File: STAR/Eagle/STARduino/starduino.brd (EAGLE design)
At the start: 59.7 x 38.2 mm, 52 parts, among them J1 J30J-25, U1 PCA9515A, U10 PCA9306DCT, U11 CC2, U12 SSCMNNN015PA2A3, U2 ATSAMD21G18, U3 MAX31725MTA+, U4 MC74VHC1GT125, U5 DS3231MZ+, U6 MC14504BDTG, U7 BMX055, U8 ADXL375BCCZ, U9 TCA9535_RTW_24

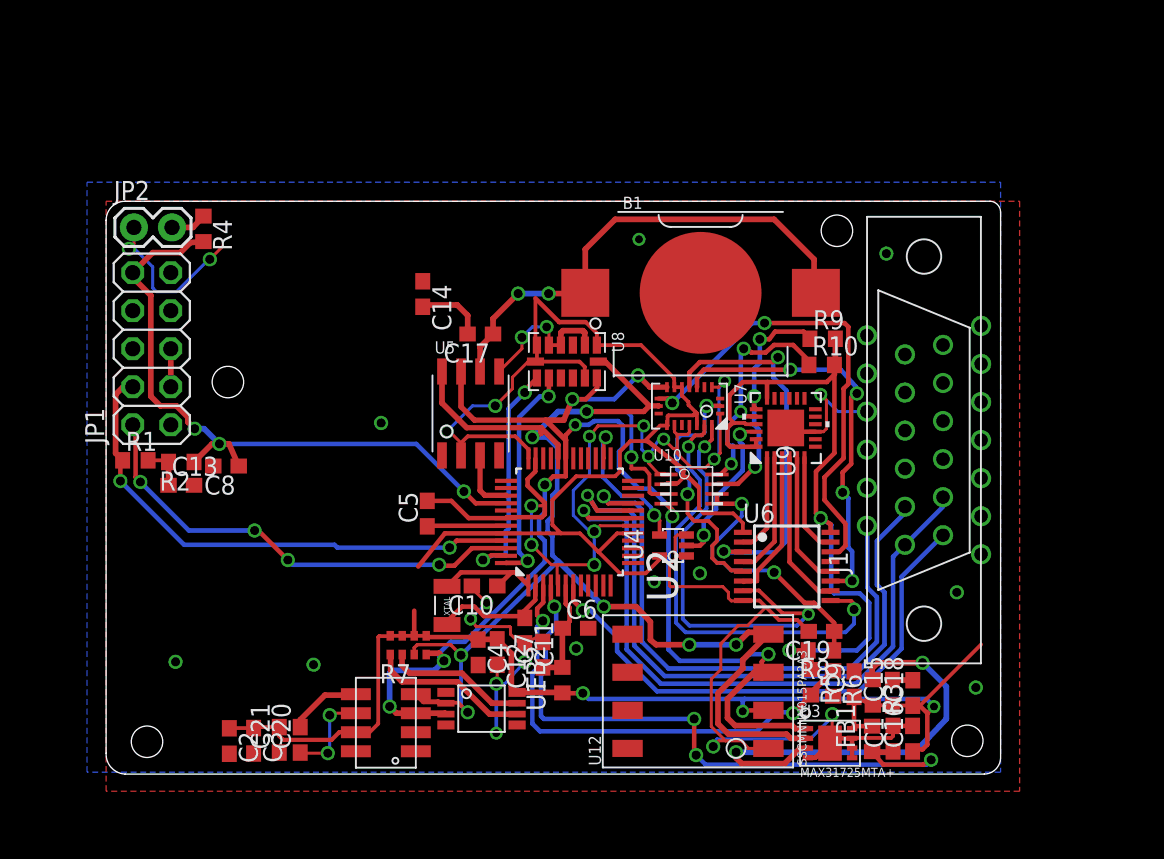
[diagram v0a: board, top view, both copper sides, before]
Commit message: new board sizes
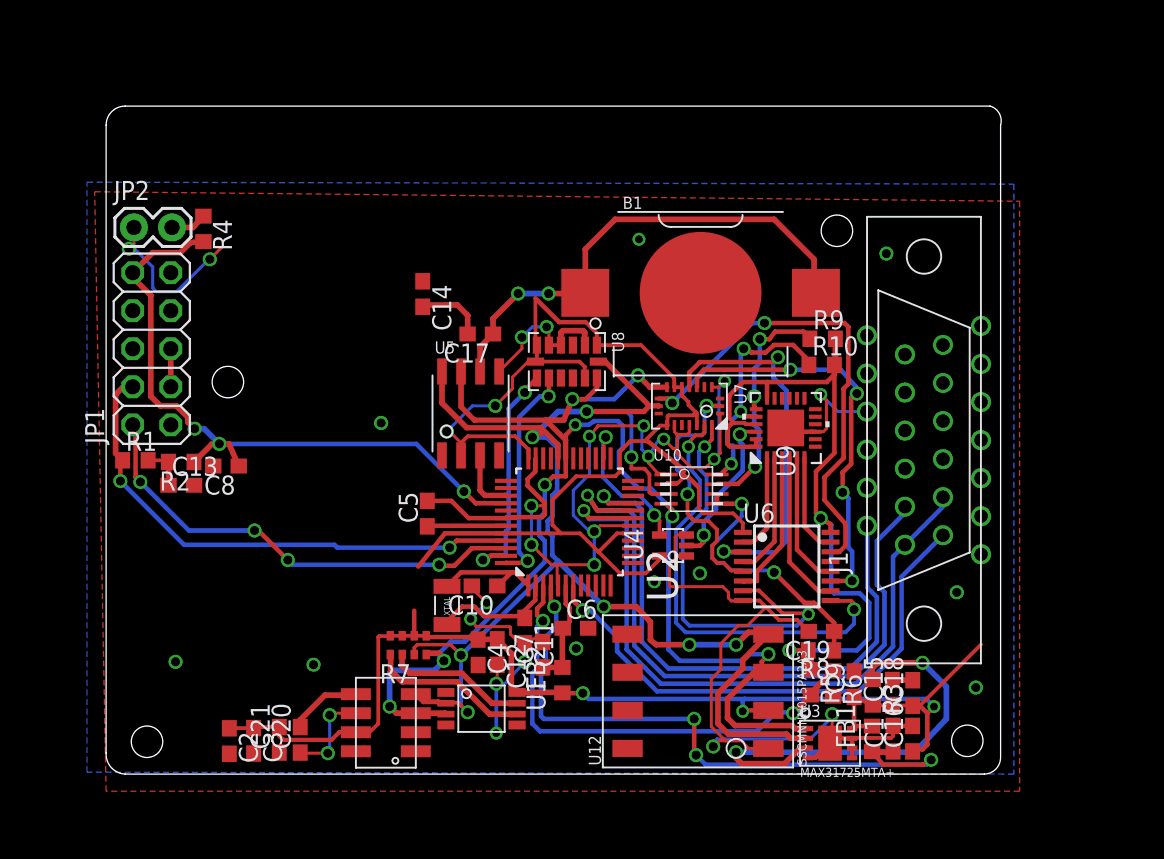
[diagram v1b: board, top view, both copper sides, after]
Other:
- board size 59.7 x 38.2 mm -> 59.7 x 44.6 mm
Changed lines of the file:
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@@
 <plain>
 <wire x1="1.27" y1="-0.127" x2="58.6105" y2="-0.127" width="0" layer="20"/>
-<wire x1="59.69" y1="1.016" x2="59.69" y2="37.338" width="0" layer="20"/>
+<wire x1="59.69" y1="1.016" x2="59.69" y2="43.18" width="0" layer="20"/>
 <dimension x1="101.6" y1="0" x2="101.6" y2="38.1" x3="106.68" y3="19.05" textsize="1.778" layer="49" unit="inch"/>
 <dimension x1="101.6" y1="38.1" x2="0" y2="38.1" x3="50.8" y3="41.91" textsize="1.778" layer="49" unit="inch"/>
 <wire x1="59.69" y1="1.016" x2="58.6105" y2="-0.127" width="0" layer="20" curve="-90"/>
-<wire x1="58.9915" y1="38.1" x2="59.69" y2="37.338" width="0" layer="20" curve="-90"/>
-<wire x1="0" y1="36.83" x2="1.27" y2="38.1" width="0" layer="20" curve="-90"/>
+<wire x1="58.9915" y1="44.45" x2="59.69" y2="43.18" width="0" layer="20" curve="-90"/>
+<wire x1="0" y1="43.18" x2="1.27" y2="44.45" width="0" layer="20" curve="-90"/>
 <wire x1="1.27" y1="-0.127" x2="0" y2="1.27" width="0" layer="20" curve="-90"/>
 <text x="25.161875" y="6.588125" size="1.27" layer="22" font="vector" rot="MR0">UMD Nearspace
@@
 <hole x="57.4675" y="2.0955" drill="2.1"/>
 <hole x="2.7305" y="2.032" drill="2.1"/>
-<wire x1="0" y1="1.27" x2="0" y2="36.83" width="0" layer="20"/>
-<wire x1="1.27" y1="38.1" x2="58.9915" y2="38.1" width="0" layer="20"/>
+<wire x1="0" y1="1.27" x2="0" y2="43.18" width="0" layer="20"/>
+<wire x1="1.27" y1="44.45" x2="58.9915" y2="44.45" width="0" layer="20"/>
 <circle x="8.128" y="26.035" radius="1.9" width="0.4064" layer="51"/>
 <circle x="2.7305" y="2.032" radius="1.9" width="0.4064" layer="51"/>
@@
 <polygon width="0.4064" layer="16">
 <vertex x="-1.27" y="39.37"/>
-<vertex x="59.69" y="39.37"/>
-<vertex x="59.69" y="0"/>
+<vertex x="60.579" y="39.243"/>
+<vertex x="60.579" y="-0.127"/>
 <vertex x="-1.27" y="0"/>
 </polygon>
 <polygon width="0.4064" layer="1">
-<vertex x="0" y="38.1"/>
+<vertex x="-0.762" y="38.735"/>
 <vertex x="60.96" y="38.1"/>
 <vertex x="60.96" y="-1.27"/>

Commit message: Power Board
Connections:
- removed net EN_28V: U2.41
- removed net I_SENSE: U2.10
- removed net LED_CTRL: U2.14
- removed net PB22: U2.37
- removed net PB23: U2.38
- removed net PI_KILL: U2.25
- removed net RX0: U2.16
- removed net RX1: U2.28
- removed net RX2: U2.30
- removed net STEPFREQ: U2.13
- removed net SYNC: U2.24
- removed net TX0: U2.15
- removed net TX1: U2.27
- removed net TX2: U2.29
- removed net USB_D_N: U2.33
- removed net USB_D_P: U2.34
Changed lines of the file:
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@@
 <wire x1="39.243" y1="1.27" x2="39.37" y2="1.143" width="0.3048" layer="1"/>
-</signal>
-<signal name="I_SENSE" class="2">
-<contactref element="U2" pad="10"/>
 </signal>
 <signal name="MISO">
@@
 <wire x1="37.5285" y1="6.9215" x2="49.657" y2="6.9215" width="0.3048" layer="16"/>
 <wire x1="49.657" y1="6.9215" x2="51.435" y2="8.6995" width="0.3048" layer="16"/>
-</signal>
-<signal name="TX1">
-<contactref element="U2" pad="27"/>
-</signal>
-<signal name="RX1">
-<contactref element="U2" pad="28"/>
 </signal>
 <signal name="NFAULT">
@@
 <wire x1="37.2745" y1="6.4135" x2="49.8475" y2="6.4135" width="0.3048" layer="16"/>
 </signal>
-<signal name="PB22">
-<contactref element="U2" pad="37"/>
-</signal>
-<signal name="PB23">
-<contactref element="U2" pad="38"/>
-</signal>
 <signal name="N$6">
 <contactref element="U3" pad="3"/>
@@
 <wire x1="32.02425" y1="32.0675" x2="31.976625" y2="31.988125" width="0.381" layer="1"/>
 </signal>
-<signal name="TX0">
-<contactref element="U2" pad="15"/>
-</signal>
-<signal name="RX0">
-<contactref element="U2" pad="16"/>
-</signal>
 <signal name="NSLEEP">
 <contactref element="U9" pad="14"/>
-</signal>
-<signal name="STEPFREQ">
-<contactref element="U2" pad="13"/>
 </signal>
 <signal name="NENBL">
@@
 <wire x1="26.6954" y1="13.97" x2="26.6827" y2="13.9573" width="0.3048" layer="1"/>
 </signal>
-<signal name="TX2">
-<contactref element="U2" pad="29"/>
-</signal>
-<signal name="RX2">
-<contactref element="U2" pad="30"/>
-</signal>
 <signal name="DEC0">
 <contactref element="U9" pad="15"/>
@@
 <signal name="DEC1">
 <contactref element="U9" pad="13"/>
-</signal>
-<signal name="LED_CTRL">
-<contactref element="U2" pad="14"/>
-</signal>
-<signal name="SYNC">
-<contactref element="U2" pad="24"/>
-</signal>
-<signal name="PI_KILL">
-<contactref element="U2" pad="25"/>
 </signal>
 <signal name="SCL_BUFF">
@@
 <wire x1="18.9865" y1="6.7945" x2="18.9865" y2="7.827" width="0.381" layer="1"/>
 <wire x1="18.9865" y1="7.827" x2="18.96125" y2="7.85225" width="0.381" layer="1"/>
-</signal>
-<signal name="EN_28V">
-<contactref element="U2" pad="41"/>
 </signal>
 <signal name="V_SENSE">
@@
 <wire x1="47.037625" y1="5.295" x2="48.514" y2="6.771375" width="0.381" layer="1"/>
 </signal>
-<signal name="USB_D_P">
-<contactref element="U2" pad="34"/>
-</signal>
-<signal name="USB_D_N">
-<contactref element="U2" pad="33"/>
-</signal>
 <signal name="5V_S">

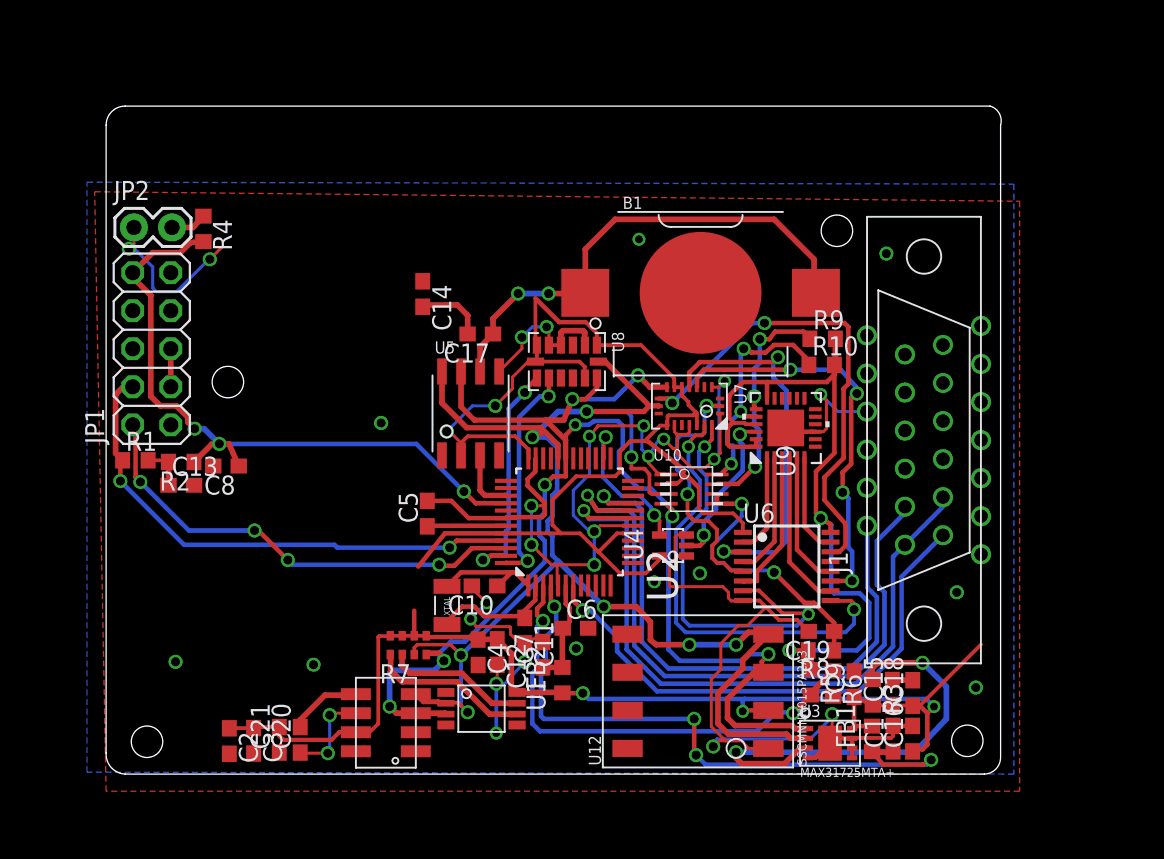
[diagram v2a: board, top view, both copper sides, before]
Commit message: fixed choke routing on power board
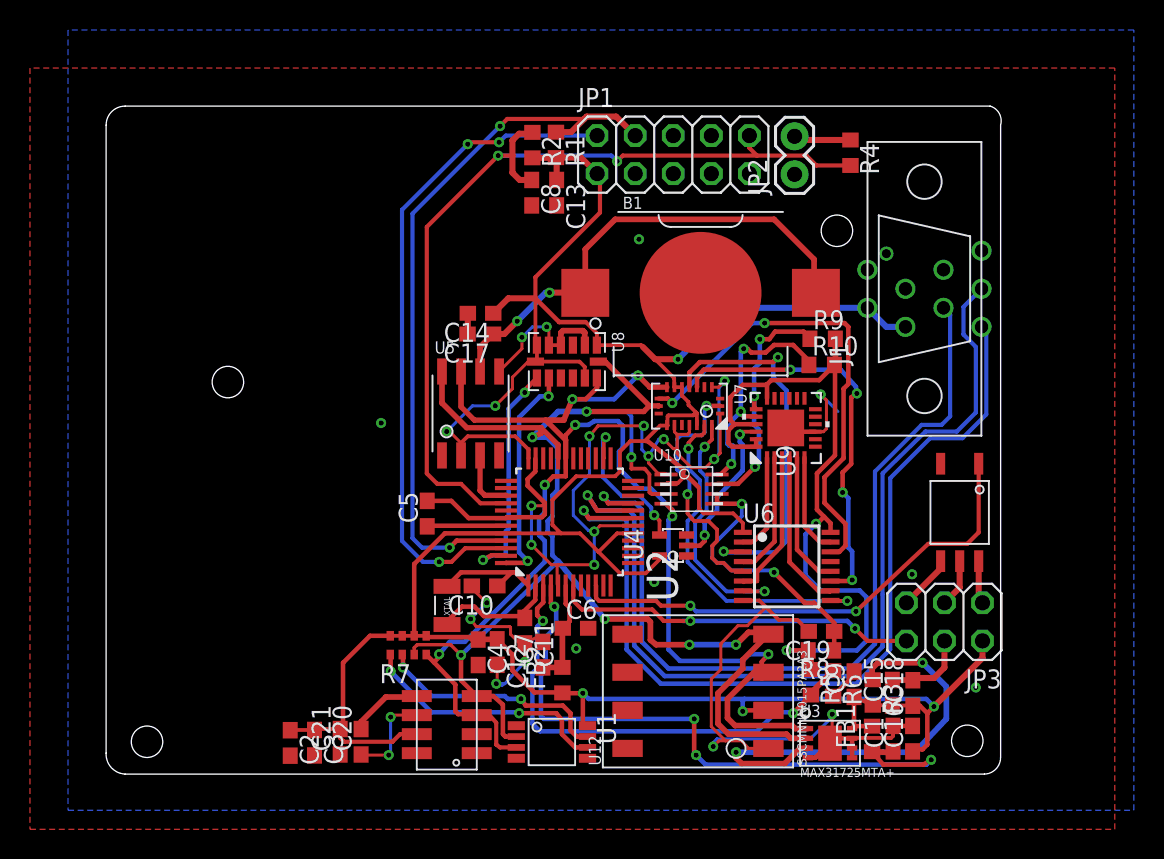
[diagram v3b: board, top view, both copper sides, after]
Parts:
- added JP3: (no value), pinhead:2X03
- added U$1: FODM8061-D, optoisolater:SO5
- J1: value J30J-25 -> J30J-9J30J; device CM_J30J:ZKN-25 -> CM_J30J:ZKN-9
- moved JP2 44.2 mm to (45.9, 39.9), turned to 90 degrees
- moved R4 43.5 mm to (49.7, 41.3)
- moved JP1 37.1 mm to (37.8, 41.2), turned to 0 degrees
- moved R1 35.1 mm to (30.0, 41.9), turned to 270 degrees
- moved C13 31.8 mm to (30.1, 38.7), turned to 270 degrees
- moved R2 31.6 mm to (28.4, 41.8), turned to 270 degrees
- moved C8 27.4 mm to (28.4, 38.7), turned to 270 degrees
- moved J1 10.1 mm to (54.6, 32.3)
- moved U1 5.20 mm to (29.7, 2.02)
- moved C14 4.07 mm to (25.0, 30.6), turned to 180 degrees
- moved C2 4.07 mm to (12.3, 1.95)
- moved C20 4.07 mm to (17.0, 2.03)
- moved C21 4.07 mm to (15.6, 2.03)
- moved C3 4.07 mm to (13.9, 1.97)
- moved U11 4.07 mm to (22.7, 3.17)
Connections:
- removed net DEC0: U9.15
- removed net DEC1: U9.13
- removed net DIR: U9.12
- removed net I0: U9.17
- removed net I1: U9.16
- removed net M0: U9.11
- removed net M1: U9.10
- removed net NENBL: U9.8
- removed net NFAULT: U9.7
- removed net NSLEEP: U9.14
- removed net SD_STAR: J1.9
- removed net VDD: J1.25
- new net MOTOR: U$1.P$1, U2.10
- new net MOTOR_GND: JP3.5, U$1.P$4
- new net MOTOR_SIGNAL: JP3.3, U$1.P$5
- new net MOTOR_VCC: JP3.1, U$1.P$6
- net +3V3: now also J1.6, J1.8, JP3.2; no longer J1.3
- net BIAS_REF: now also JP3.6; no longer J1.2
- net GND: now also J1.5, JP3.4, U$1.P$3; no longer J1.21, J1.22, J1.23, J1.24
- net MISO: now also J1.2; no longer J1.15
- net MOSI: now also J1.1; no longer J1.14
- net SCK: now also J1.3; no longer J1.16
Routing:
- net +3V3: track 173.4 -> 215.2 mm, vias 5 -> 6
- net MOTOR: track 0.00 -> 33.4 mm, vias 0 -> 2
- net GND: track 181.3 -> 154.9 mm, vias 34 -> 28
- net SCK: track 44.7 -> 62.9 mm
- net MISO: track 39.2 -> 56.4 mm
- net RESET: track 45.6 -> 61.1 mm, vias 3 -> 2
- net MOSI: track 45.9 -> 60.5 mm
- net SWDIO: track 31.2 -> 45.1 mm, vias 4 -> 3
- net SWDCLK: track 35.2 -> 48.7 mm
- net IMUINT2: track 28.1 -> 16.8 mm
- net BIAS_REF: track 35.8 -> 24.9 mm, vias 1 -> 2
- net IMUDR: track 30.2 -> 23.4 mm
- net SCL_BUFF: track 9.46 -> 15.8 mm, vias 0 -> 2
- net SDA_BUFF: track 10.7 -> 17.0 mm, vias 0 -> 2
- net MOTOR_GND: track 0.00 -> 3.73 mm
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
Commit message: gerbers for boards
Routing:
- net GND: vias 28 -> 41
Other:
- board text added: "2018STARduino Rev. 2"
- board text removed: "2018STARduino Rev. 1"
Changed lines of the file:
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@@
 <layer number="20" name="Dimension" color="15" fill="1" visible="yes" active="yes"/>
 <layer number="21" name="tPlace" color="7" fill="1" visible="yes" active="yes"/>
-<layer number="22" name="bPlace" color="7" fill="1" visible="no" active="yes"/>
+<layer number="22" name="bPlace" color="7" fill="1" visible="yes" active="yes"/>
 <layer number="23" name="tOrigins" color="15" fill="1" visible="yes" active="yes"/>
 <layer number="24" name="bOrigins" color="15" fill="1" visible="yes" active="yes"/>
@@
 <text x="56.35625" y="39.37" size="1.27" layer="161" font="vector">FDG8842</text>
 <text x="64.29375" y="41.513125" size="1.27" layer="161" font="vector">P82B75</text>
-<text x="25.320625" y="4.7625" size="1.27" layer="22" font="vector" rot="MR0">2018STARduino Rev. 1</text>
+<text x="25.320625" y="4.7625" size="1.27" layer="22" font="vector" rot="MR0">2018STARduino Rev. 2</text>
 <hole x="8.128" y="26.035" drill="2.1"/>
 <hole x="48.768" y="36.1315" drill="2.1"/>
@@
 <vertex x="67.31" y="46.99"/>
 </polygon>
-<wire x1="49.911" y1="6.72375" x2="49.911" y2="6.468375" width="0.3048" layer="1"/>
-<wire x1="49.911" y1="6.468375" x2="48.514" y2="5.071375" width="0.3048" layer="1"/>
+<wire x1="49.911" y1="6.72375" x2="49.911" y2="6.595375" width="0.3048" layer="1"/>
+<wire x1="49.911" y1="6.595375" x2="48.514" y2="5.071375" width="0.3048" layer="1"/>
+<via x="4.699" y="39.8145" extent="1-16" drill="0.3302"/>
+<via x="16.1925" y="40.005" extent="1-16" drill="0.3302"/>
+<via x="15.748" y="29.464" extent="1-16" drill="0.3302"/>
+<via x="3.4925" y="29.083" extent="1-16" drill="0.3302"/>
+<via x="4.953" y="19.1135" extent="1-16" drill="0.3302"/>
+<via x="10.16" y="16.383" extent="1-16" drill="0.3302"/>
+<via x="17.0815" y="13.335" extent="1-16" drill="0.3302"/>
+<via x="4.572" y="10.541" extent="1-16" drill="0.3302"/>
+<via x="11.557" y="6.604" extent="1-16" drill="0.3302"/>
+<via x="53.7845" y="17.5895" extent="1-16" drill="0.3302"/>
+<via x="52.2605" y="25.4" extent="1-16" drill="0.3302"/>
+<via x="56.3245" y="40.9575" extent="1-16" drill="0.3302"/>
+<via x="24.892" y="35.306" extent="1-16" drill="0.3302"/>
 </signal>
 <signal name="N$5">

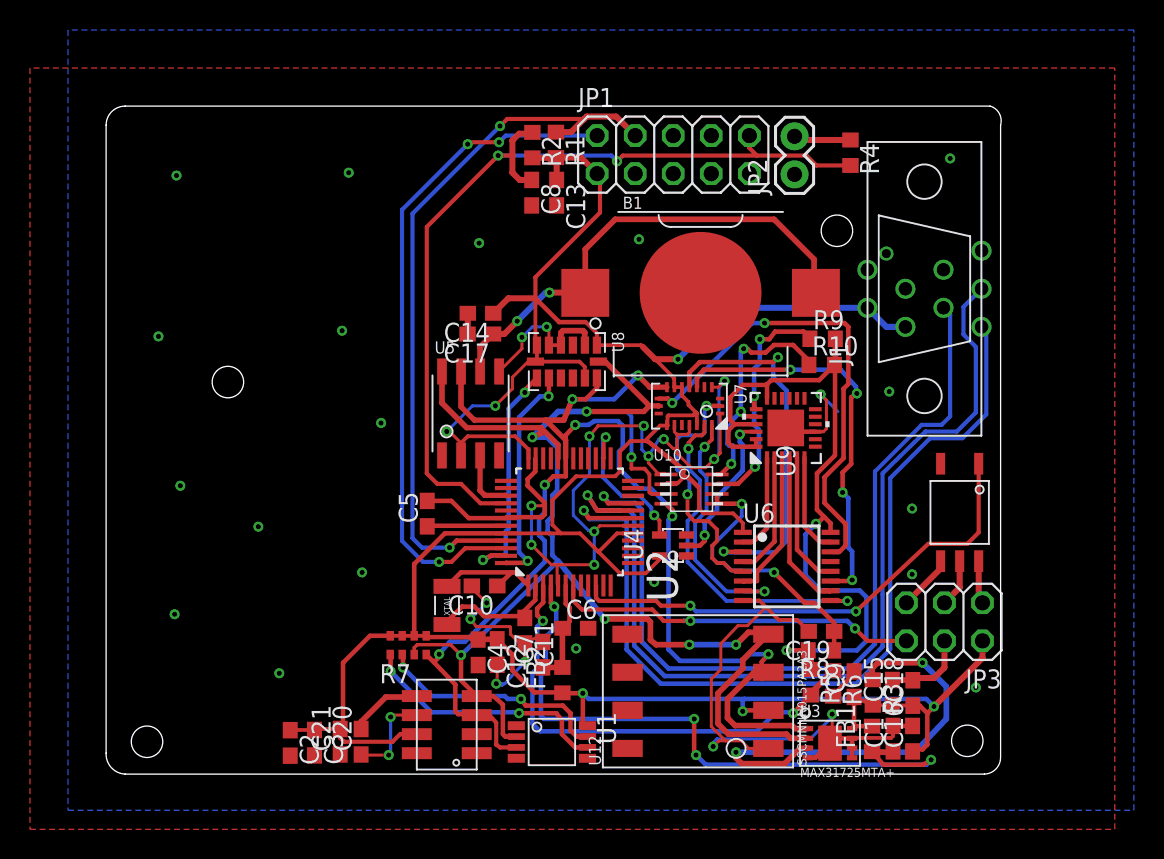
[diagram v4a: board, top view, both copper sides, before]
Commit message: Fixed all the wire stubs on Starduino
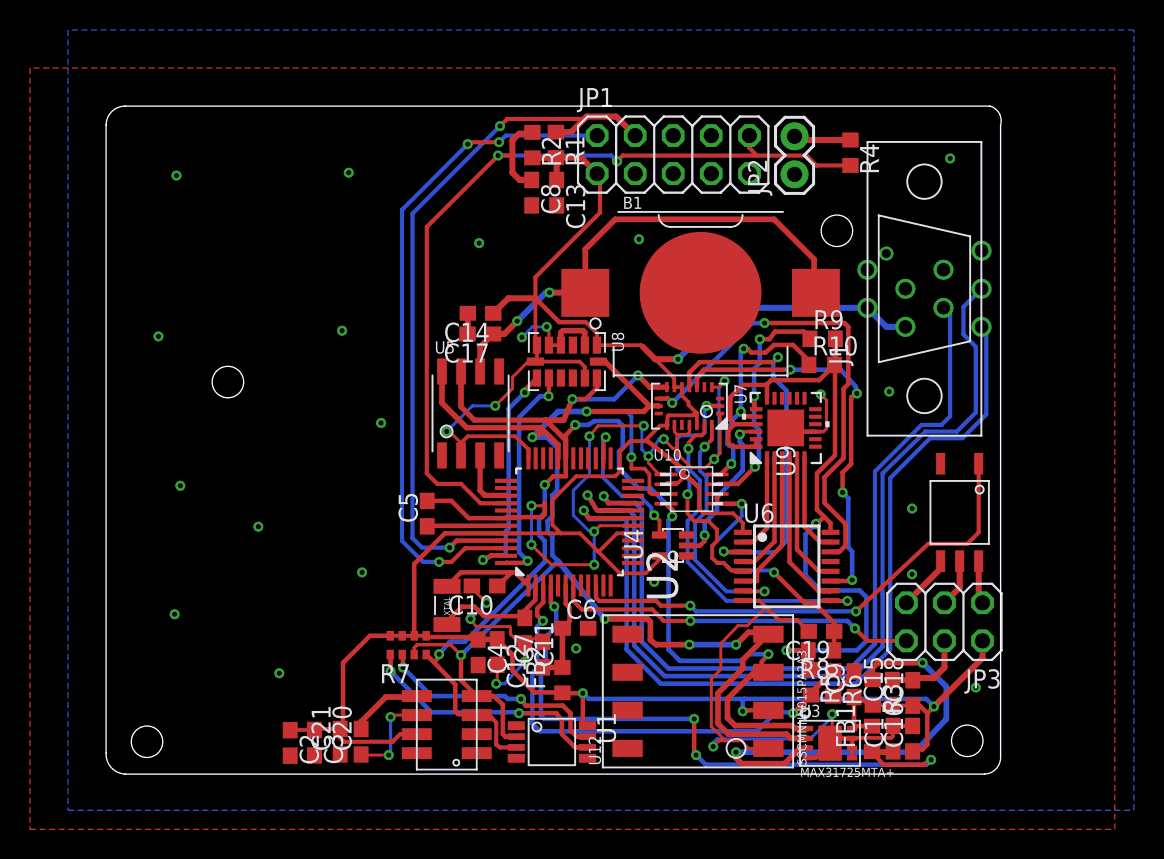
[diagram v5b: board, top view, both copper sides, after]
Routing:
- net GND: track 154.9 -> 143.2 mm
- net +3V3: track 215.2 -> 214.3 mm
- net SDA: track 96.6 -> 96.1 mm
- net BIAS_REF: track 24.9 -> 24.4 mm
